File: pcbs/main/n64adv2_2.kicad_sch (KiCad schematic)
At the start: 70 parts, among them U10 TLV70225DBVR, U11 TLV70025

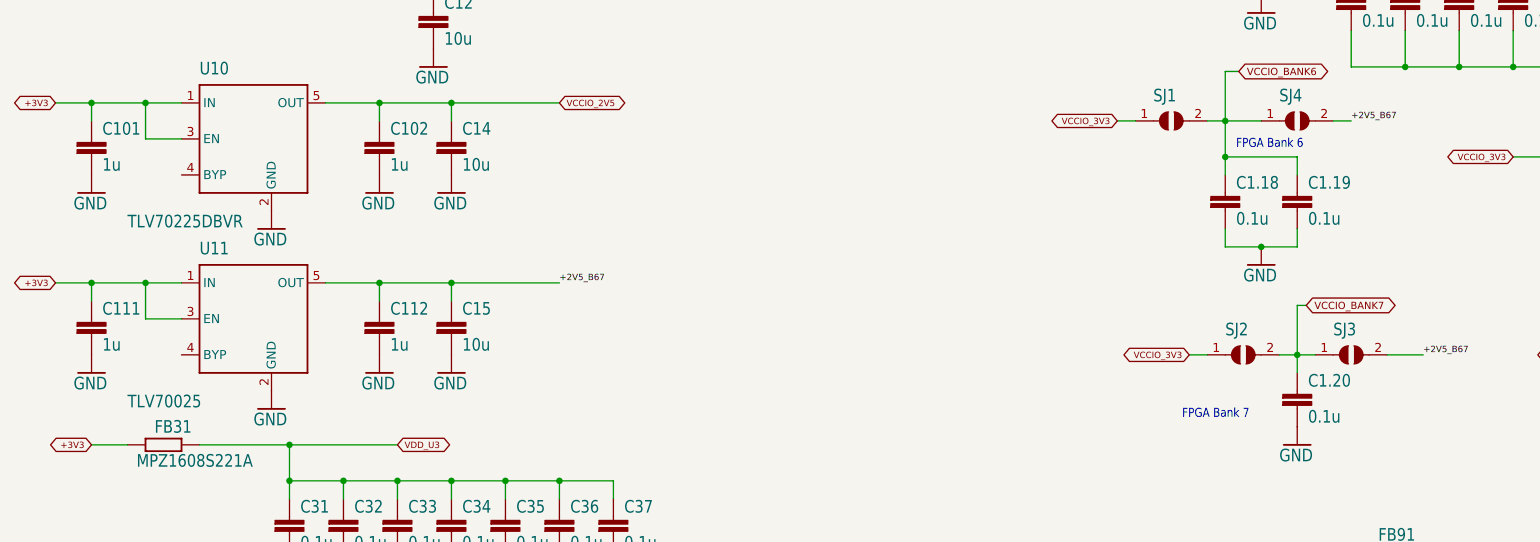
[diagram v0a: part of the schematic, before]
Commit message: update main PCB with minor changes, e.g. ensure that solder mask bridges between 0.5mm pitched pads has min. 0.1mm thickness
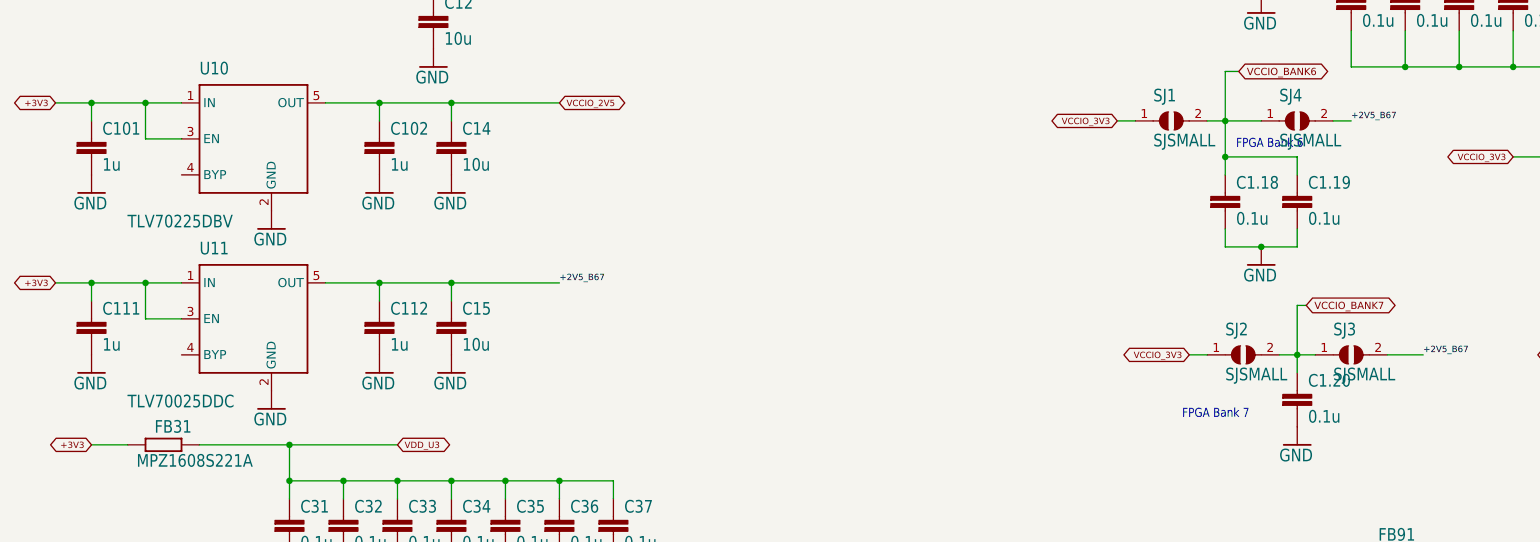
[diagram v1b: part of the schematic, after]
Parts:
- P_GND_3, UNK3V_IN0: value (none) -> SMD2; footprint (none) -> n64adv2:SMD1,27-2,54
- SF_GND_1, SF_GND_2: value (none) -> PADSHIELD_FINGER; footprint (none) -> n64adv2:GND_FINGER_PAD
- SJ1, SJ2, SJ3, SJ4: value (none) -> SJSMALL; footprint (none) -> n64adv2:SJ_SMALL
- U10: value TLV70225DBVR -> TLV70225DBV
- U11: value TLV70025 -> TLV70025DDC
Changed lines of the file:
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@@
       (effects (font (size 1.778 1.5113)) (justify left bottom))
     )
-    (property "Value" "" (id 1) (at 37.338 26.797 0)
+    (property "Value" "SMD2" (id 1) (at 37.338 26.797 0)
       (effects (font (size 1.778 1.5113)) (justify left bottom) hide)
     )
-    (property "Footprint" "" (id 2) (at 40.64 27.94 0)
+    (property "Footprint" "n64adv2:SMD1,27-2,54" (id 2) (at 40.64 27.94 0)
       (effects (font (size 1.27 1.27)) hide)
     )
@@
       (effects (font (size 1.778 1.5113)) (justify left bottom))
     )
-    (property "Value" "" (id 1) (at 60.96 45.72 0)
+    (property "Value" "PADSHIELD_FINGER" (id 1) (at 60.96 45.72 0)
       (effects (font (size 1.778 1.5113)) (justify left bottom) hide)
     )
-    (property "Footprint" "" (id 2) (at 55.88 43.18 0)
+    (property "Footprint" "n64adv2:GND_FINGER_PAD" (id 2) (at 55.88 43.18 0)
       (effects (font (size 1.27 1.27)) hide)
     )
@@
       (effects (font (size 1.778 1.5113)) (justify left bottom))
     )
-    (property "Value" "" (id 1) (at 58.42 45.72 0)
+    (property "Value" "PADSHIELD_FINGER" (id 1) (at 58.42 45.72 0)
       (effects (font (size 1.778 1.5113)) (justify left bottom) hide)
     )
-    (property "Footprint" "" (id 2) (at 53.34 43.18 0)
+    (property "Footprint" "n64adv2:GND_FINGER_PAD" (id 2) (at 53.34 43.18 0)
       (effects (font (size 1.27 1.27)) hide)
     )
@@
       (effects (font (size 1.778 1.5113)) (justify left bottom))
     )
-    (property "Value" "TLV70025" (id 1) (at 33.02 124.46 0)
+    (property "Value" "TLV70025DDC" (id 1) (at 33.02 124.46 0)
       (effects (font (size 1.778 1.5113)) (justify left bottom))
     )
@@
       (effects (font (size 1.778 1.5113)) (justify left bottom))
     )
-    (property "Value" "" (id 1) (at 195.58 87.63 0)
-      (effects (font (size 1.778 1.5113)) (justify left bottom))
-    )
-    (property "Footprint" "" (id 2) (at 198.12 83.82 0)
+    (property "Value" "SJSMALL" (id 1) (at 195.58 87.63 0)
+      (effects (font (size 1.778 1.5113)) (justify left bottom))
+    )
+    (property "Footprint" "n64adv2:SJ_SMALL" (id 2) (at 198.12 83.82 0)
       (effects (font (size 1.27 1.27)) hide)
     )
@@
       (effects (font (size 1.778 1.5113)) (justify left bottom))
     )
-    (property "Value" "" (id 1) (at 203.2 120.65 0)
-      (effects (font (size 1.778 1.5113)) (justify left bottom))
-    )
-    (property "Footprint" "" (id 2) (at 205.74 116.84 0)
+    (property "Value" "SJSMALL" (id 1) (at 203.2 120.65 0)
+      (effects (font (size 1.778 1.5113)) (justify left bottom))
+    )
+    (property "Footprint" "n64adv2:SJ_SMALL" (id 2) (at 205.74 116.84 0)
       (effects (font (size 1.27 1.27)) hide)
     )
@@
       (effects (font (size 1.778 1.5113)) (justify left bottom))
     )
-    (property "Value" "" (id 1) (at 177.8 87.63 0)
-      (effects (font (size 1.778 1.5113)) (justify left bottom))
-    )
-    (property "Footprint" "" (id 2) (at 180.34 83.82 0)
+    (property "Value" "SJSMALL" (id 1) (at 177.8 87.63 0)
+      (effects (font (size 1.778 1.5113)) (justify left bottom))
+    )
+    (property "Footprint" "n64adv2:SJ_SMALL" (id 2) (at 180.34 83.82 0)
       (effects (font (size 1.27 1.27)) hide)
     )
@@
       (effects (font (size 1.778 1.5113)) (justify left bottom))
     )
-    (property "Value" "TLV70225DBVR" (id 1) (at 33.02 99.06 0)
+    (property "Value" "TLV70225DBV" (id 1) (at 33.02 99.06 0)
       (effects (font (size 1.778 1.5113)) (justify left bottom))
     )
@@
       (effects (font (size 1.778 1.5113)) (justify left bottom))
     )
-    (property "Value" "" (id 1) (at 187.96 120.65 0)
-      (effects (font (size 1.778 1.5113)) (justify left bottom))
-    )
-    (property "Footprint" "" (id 2) (at 190.5 116.84 0)
+    (property "Value" "SJSMALL" (id 1) (at 187.96 120.65 0)
+      (effects (font (size 1.778 1.5113)) (justify left bottom))
+    )
+    (property "Footprint" "n64adv2:SJ_SMALL" (id 2) (at 190.5 116.84 0)
       (effects (font (size 1.27 1.27)) hide)
     )
@@
       (effects (font (size 1.778 1.5113)) (justify left bottom))
     )
-    (property "Value" "" (id 1) (at 54.102 49.403 0)
+    (property "Value" "SMD2" (id 1) (at 54.102 49.403 0)
       (effects (font (size 1.778 1.5113)) (justify left bottom) hide)
     )
-    (property "Footprint" "" (id 2) (at 50.8 48.26 0)
-      (effects (font (size 1.27 1.27)) hide)
-    )
+    (property "Footprint" "n64adv2:SMD1,27-2,54" (id 2) (at 50.8 48.26 0)
+      (effects (font (size 1.27 1.27)) hide)
+    )

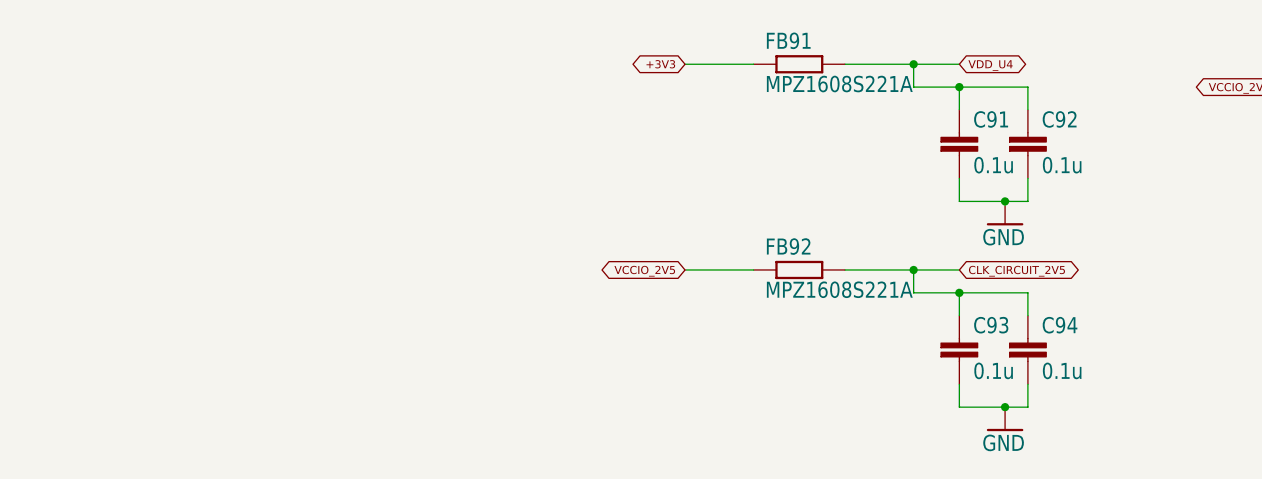
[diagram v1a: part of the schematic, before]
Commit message: update main PCB: - optimize some trace routing - optimize component selection/placing (e.g. HDMI port full SMD, JTAG as SMD alternative) - add license to silkscreen
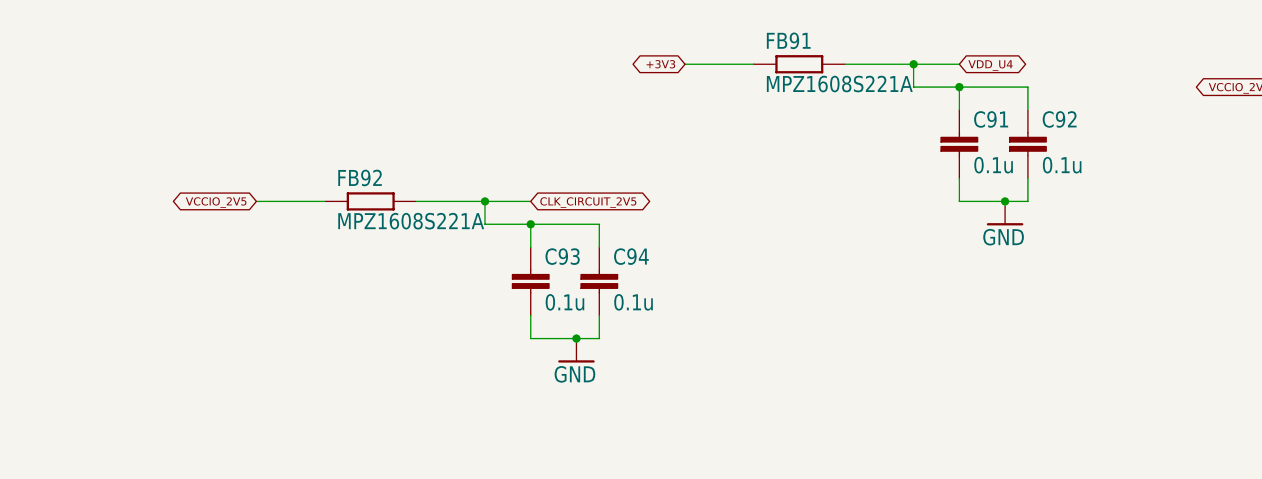
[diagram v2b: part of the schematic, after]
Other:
- company: (none) -> Peter 'borti4938' Bartmann
- title: (none) -> N64Adv2 (ADV7513)
- moved on the sheet: C93, C94, FB92
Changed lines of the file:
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@@
 (kicad_sch (version 20211123) (generator eeschema)
   (paper "User" 326.542 210.007)
+  (title_block
+    (title "N64Adv2 (ADV7513)")
+    (rev "v20220729")
+    (company "Peter 'borti4938' Bartmann")
+    (comment 1 "Schematic and PCB (c) 2021, 2022 by Peter Bartmann")
+    (comment 2 "N64Adv2_20220729")
+    (comment 3 "Licensed under CERN-OHL-W v2")
+  )
   (junction (at 53.34 45.72) (diameter 0) (color 0 0 0 0)
   )
-  (junction (at 236.22 182.88) (diameter 0) (color 0 0 0 0)
+  (junction (at 188.595 175.26) (diameter 0) (color 0 0 0 0)
   )
   (junction (at 236.22 76.2) (diameter 0) (color 0 0 0 0)
@@
   (junction (at 220.98 76.2) (diameter 0) (color 0 0 0 0)
   )
-  (junction (at 231.14 170.18) (diameter 0) (color 0 0 0 0)
+  (junction (at 183.515 162.56) (diameter 0) (color 0 0 0 0)
   )
   (junction (at 193.04 55.88) (diameter 0) (color 0 0 0 0)
@@
   (junction (at 256.54 116.84) (diameter 0) (color 0 0 0 0)
   )
-  (junction (at 226.06 167.64) (diameter 0) (color 0 0 0 0)
+  (junction (at 178.435 160.02) (diameter 0) (color 0 0 0 0)
   )
   (junction (at 33.02 45.72) (diameter 0) (color 0 0 0 0)
@@
     (stroke (width 0) (type default) (color 0 0 0 0))
   )
-  (wire (pts (xy 231.14 170.18) (xy 238.76 170.18))
+  (wire (pts (xy 183.515 162.56) (xy 191.135 162.56))
     (stroke (width 0) (type default) (color 0 0 0 0))
   )
@@
     (stroke (width 0) (type default) (color 0 0 0 0))
   )
-  (wire (pts (xy 231.14 182.88) (xy 236.22 182.88))
+  (wire (pts (xy 183.515 175.26) (xy 188.595 175.26))
     (stroke (width 0) (type default) (color 0 0 0 0))
   )
@@
     (stroke (width 0) (type default) (color 0 0 0 0))
   )
-  (wire (pts (xy 238.76 182.88) (xy 238.76 180.34))
+  (wire (pts (xy 191.135 175.26) (xy 191.135 172.72))
     (stroke (width 0) (type default) (color 0 0 0 0))
   )
@@
     (stroke (width 0) (type default) (color 0 0 0 0))
   )
-  (wire (pts (xy 226.06 167.64) (xy 226.06 170.18))
+  (wire (pts (xy 178.435 160.02) (xy 178.435 162.56))
     (stroke (width 0) (type default) (color 0 0 0 0))
   )
@@
     (stroke (width 0) (type default) (color 0 0 0 0))
   )
-  (wire (pts (xy 226.06 167.64) (xy 231.14 167.64))
+  (wire (pts (xy 178.435 160.02) (xy 183.515 160.02))
     (stroke (width 0) (type default) (color 0 0 0 0))
   )
@@
     (stroke (width 0) (type default) (color 0 0 0 0))
   )
-  (wire (pts (xy 200.66 167.64) (xy 208.28 167.64))
+  (wire (pts (xy 153.035 160.02) (xy 160.655 160.02))
     (stroke (width 0) (type default) (color 0 0 0 0))
   )
@@
     (stroke (width 0) (type default) (color 0 0 0 0))
   )
-  (wire (pts (xy 238.76 170.18) (xy 238.76 172.72))
+  (wire (pts (xy 191.135 162.56) (xy 191.135 165.1))
     (stroke (width 0) (type default) (color 0 0 0 0))
   )
@@
     (stroke (width 0) (type default) (color 0 0 0 0))
   )
-  (wire (pts (xy 218.44 167.64) (xy 226.06 167.64))
+  (wire (pts (xy 170.815 160.02) (xy 178.435 160.02))
     (stroke (width 0) (type default) (color 0 0 0 0))
   )
@@
     (stroke (width 0) (type default) (color 0 0 0 0))
   )
-  (wire (pts (xy 231.14 172.72) (xy 231.14 170.18))
+  (wire (pts (xy 183.515 165.1) (xy 183.515 162.56))
     (stroke (width 0) (type default) (color 0 0 0 0))
   )
@@
     (stroke (width 0) (type default) (color 0 0 0 0))
   )
-  (wire (pts (xy 226.06 170.18) (xy 231.14 170.18))
+  (wire (pts (xy 178.435 162.56) (xy 183.515 162.56))
     (stroke (width 0) (type default) (color 0 0 0 0))
   )
@@
     (stroke (width 0) (type default) (color 0 0 0 0))
   )
-  (wire (pts (xy 236.22 182.88) (xy 238.76 182.88))
+  (wire (pts (xy 188.595 175.26) (xy 191.135 175.26))
     (stroke (width 0) (type default) (color 0 0 0 0))
   )
@@
     (stroke (width 0) (type default) (color 0 0 0 0))
   )
-  (wire (pts (xy 231.14 180.34) (xy 231.14 182.88))
+  (wire (pts (xy 183.515 172.72) (xy 183.515 175.26))
     (stroke (width 0) (type default) (color 0 0 0 0))
   )
@@
     )
   )
-  (global_label "CLK_CIRCUIT_2V5" (shape bidirectional) (at 231.14 167.64 0) (fields_autoplaced)
+  (global_label "CLK_CIRCUIT_2V5" (shape bidirectional) (at 183.515 160.02 0) (fields_autoplaced)
     (effects (font (size 0.889 0.889)) (justify left))
-    (property "Intersheet References" "${INTERSHEET_REFS}" (id 0) (at 0 0 0)
+    (property "Intersheet References" "${INTERSHEET_REFS}" (id 0) (at -47.625 -7.62 0)
       (effects (font (size 1.27 1.27)) hide)
     )
@@
     )
   )
-  (global_label "VCCIO_2V5" (shape bidirectional) (at 200.66 167.64 180) (fields_autoplaced)
+  (global_label "VCCIO_2V5" (shape bidirectional) (at 153.035 160.02 180) (fields_autoplaced)
     (effects (font (size 0.889 0.889)) (justify right))
-    (property "Intersheet References" "${INTERSHEET_REFS}" (id 0) (at 381 30.48 0)
+    (property "Intersheet References" "${INTERSHEET_REFS}" (id 0) (at 333.375 22.86 0)
       (effects (font (size 1.27 1.27)) hide)
     )
@@
     (pin "2")
   )
-  (symbol (lib_id "n64adv2-eagle-import:R-EU_R0603") (at 213.36 167.64 0) (unit 1)
-    (in_bom yes) (on_board yes)
-    (property "Reference" "FB92" (id 0) (at 209.55 166.1414 0)
-      (effects (font (size 1.778 1.5113)) (justify left bottom))
-    )
-    (property "Value" "MPZ1608S221A" (id 1) (at 209.55 170.942 0)
-      (effects (font (size 1.778 1.5113)) (justify left bottom))
-    )
-    (property "Footprint" "n64adv2:R0603" (id 2) (at 213.36 167.64 0)
-      (effects (font (size 1.27 1.27)) hide)
-    )
-    (property "Datasheet" "" (id 3) (at 213.36 167.64 0)
+  (symbol (lib_id "n64adv2-eagle-import:R-EU_R0603") (at 165.735 160.02 0) (unit 1)
+    (in_bom yes) (on_board yes)
+    (property "Reference" "FB92" (id 0) (at 161.925 158.5214 0)
+      (effects (font (size 1.778 1.5113)) (justify left bottom))
+    )
+    (property "Value" "MPZ1608S221A" (id 1) (at 161.925 163.322 0)
+      (effects (font (size 1.778 1.5113)) (justify left bottom))
+    )
+    (property "Footprint" "n64adv2:R0603" (id 2) (at 165.735 160.02 0)
+      (effects (font (size 1.27 1.27)) hide)
+    )
+    (property "Datasheet" "" (id 3) (at 165.735 160.02 0)
       (effects (font (size 1.27 1.27)) hide)
     )
@@
     (pin "2")
   )
-  (symbol (lib_id "n64adv2-eagle-import:C-EUC0603") (at 231.14 175.26 0) (unit 1)
-    (in_bom yes) (on_board yes)
-    (property "Reference" "C93" (id 0) (at 232.664 174.879 0)
-      (effects (font (size 1.778 1.5113)) (justify left bottom))
-    )
-    (property "Value" "0.1u" (id 1) (at 232.664 179.959 0)
-      (effects (font (size 1.778 1.5113)) (justify left bottom))
-    )
-    (property "Footprint" "n64adv2:C0603" (id 2) (at 231.14 175.26 0)
-      (effects (font (size 1.27 1.27)) hide)
-    )
-    (property "Datasheet" "" (id 3) (at 231.14 175.26 0)
+  (symbol (lib_id "n64adv2-eagle-import:C-EUC0603") (at 183.515 167.64 0) (unit 1)
+    (in_bom yes) (on_board yes)
+    (property "Reference" "C93" (id 0) (at 185.039 167.259 0)
+      (effects (font (size 1.778 1.5113)) (justify left bottom))
+    )
+    (property "Value" "0.1u" (id 1) (at 185.039 172.339 0)
+      (effects (font (size 1.778 1.5113)) (justify left bottom))
+    )
+    (property "Footprint" "n64adv2:C0603" (id 2) (at 183.515 167.64 0)
+      (effects (font (size 1.27 1.27)) hide)
+    )
+    (property "Datasheet" "" (id 3) (at 183.515 167.64 0)
       (effects (font (size 1.27 1.27)) hide)
     )
@@
     (pin "2")
   )
-  (symbol (lib_id "n64adv2-eagle-import:C-EUC0603") (at 238.76 175.26 0) (unit 1)
-    (in_bom yes) (on_board yes)
-    (property "Reference" "C94" (id 0) (at 240.284 174.879 0)
-      (effects (font (size 1.778 1.5113)) (justify left bottom))
-    )
-    (property "Value" "0.1u" (id 1) (at 240.284 179.959 0)
-      (effects (font (size 1.778 1.5113)) (justify left bottom))
-    )
-    (property "Footprint" "n64adv2:C0603" (id 2) (at 238.76 175.26 0)
-      (effects (font (size 1.27 1.27)) hide)
-    )
-    (property "Datasheet" "" (id 3) (at 238.76 175.26 0)
+  (symbol (lib_id "n64adv2-eagle-import:C-EUC0603") (at 191.135 167.64 0) (unit 1)
+    (in_bom yes) (on_board yes)
+    (property "Reference" "C94" (id 0) (at 192.659 167.259 0)
+      (effects (font (size 1.778 1.5113)) (justify left bottom))
+    )
+    (property "Value" "0.1u" (id 1) (at 192.659 172.339 0)
+      (effects (font (size 1.778 1.5113)) (justify left bottom))
+    )
+    (property "Footprint" "n64adv2:C0603" (id 2) (at 191.135 167.64 0)
+      (effects (font (size 1.27 1.27)) hide)
+    )
+    (property "Datasheet" "" (id 3) (at 191.135 167.64 0)
       (effects (font (size 1.27 1.27)) hide)
     )
@@
     (pin "1")
   )
-  (symbol (lib_id "n64adv2-eagle-import:GND") (at 236.22 185.42 0) (unit 1)
-    (in_bom yes) (on_board yes)
-    (property "Reference" "#GND062" (id 0) (at 236.22 185.42 0)
-      (effects (font (size 1.27 1.27)) hide)
-    )
-    (property "Value" "GND" (id 1) (at 233.68 187.96 0)
-      (effects (font (size 1.778 1.5113)) (justify left bottom))
-    )
-    (property "Footprint" "n64adv2:" (id 2) (at 236.22 185.42 0)
-      (effects (font (size 1.27 1.27)) hide)
-    )
-    (property "Datasheet" "" (id 3) (at 236.22 185.42 0)
-      (effects (font (size 1.27 1.27)) hide)
-    )
+  (symbol (lib_id "n64adv2-eagle-import:GND") (at 188.595 177.8 0) (unit 1)
+    (in_bom yes) (on_board yes)
+    (property "Reference" "#GND062" (id 0) (at 188.595 177.8 0)
+      (effects (font (size 1.27 1.27)) hide)
+    )
+    (property "Value" "GND" (id 1) (at 186.055 180.34 0)
+      (effects (font (size 1.778 1.5113)) (justify left bottom))
+    )
+    (property "Footprint" "n64adv2:" (id 2) (at 188.595 177.8 0)
+      (effects (font (size 1.27 1.27)) hide)
+    )
+    (property "Datasheet" "" (id 3) (at 188.595 177.8 0)
+      (effects (font (size 1.27 1.27)) hide)
+    )
